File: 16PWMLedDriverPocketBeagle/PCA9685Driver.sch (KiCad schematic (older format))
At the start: 17 parts, among them P3 C A0 A1 A2 A3 A4 A5 A6 A7, P4 C B0 B1 B2 B3 B4 B5 B6 B7, U4 PCA9685, U5 TBD62X83A, U6 TBD62X83A

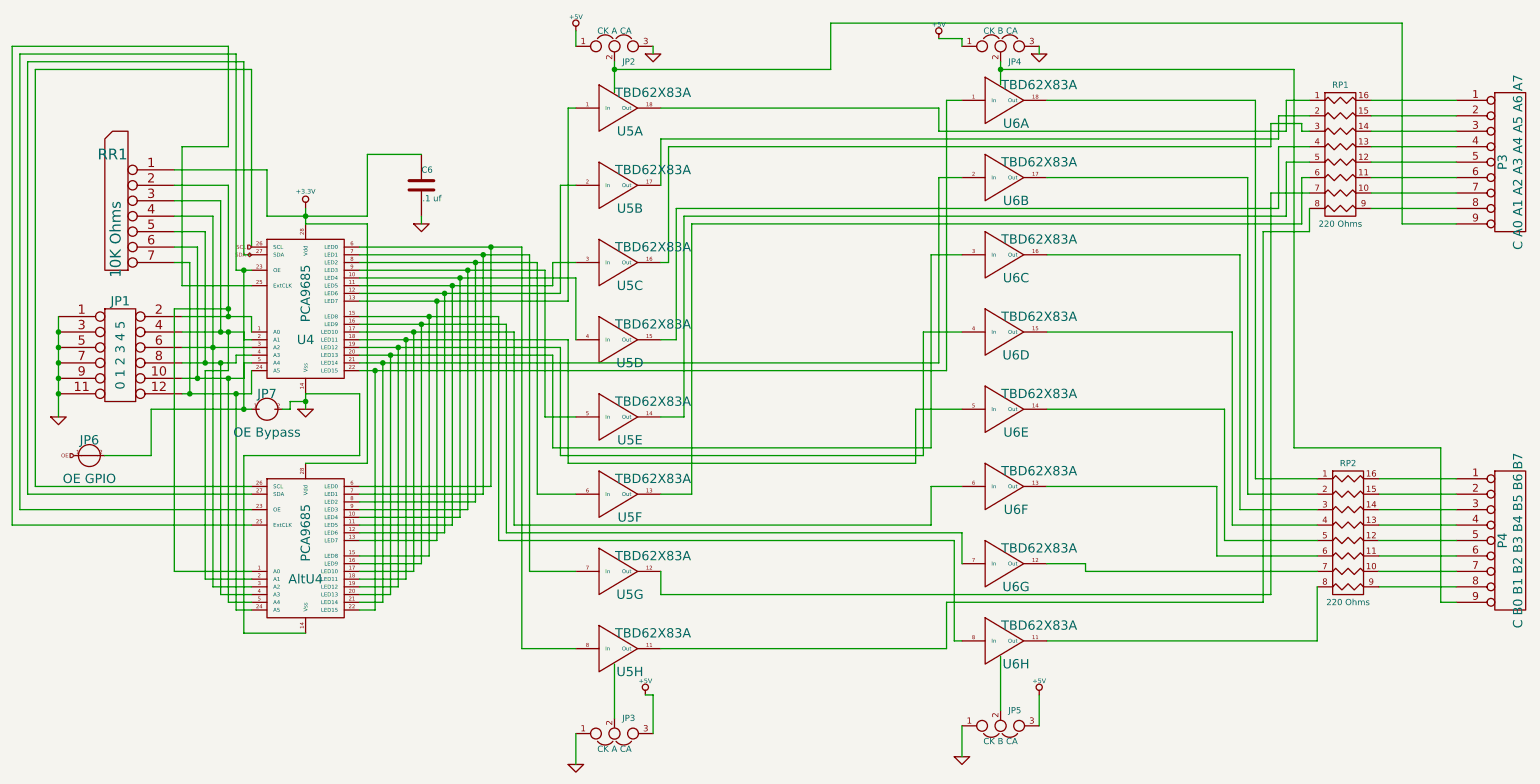
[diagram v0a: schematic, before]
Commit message: Convert the 16PWM Led Drivers to use 12V for the LEDs.
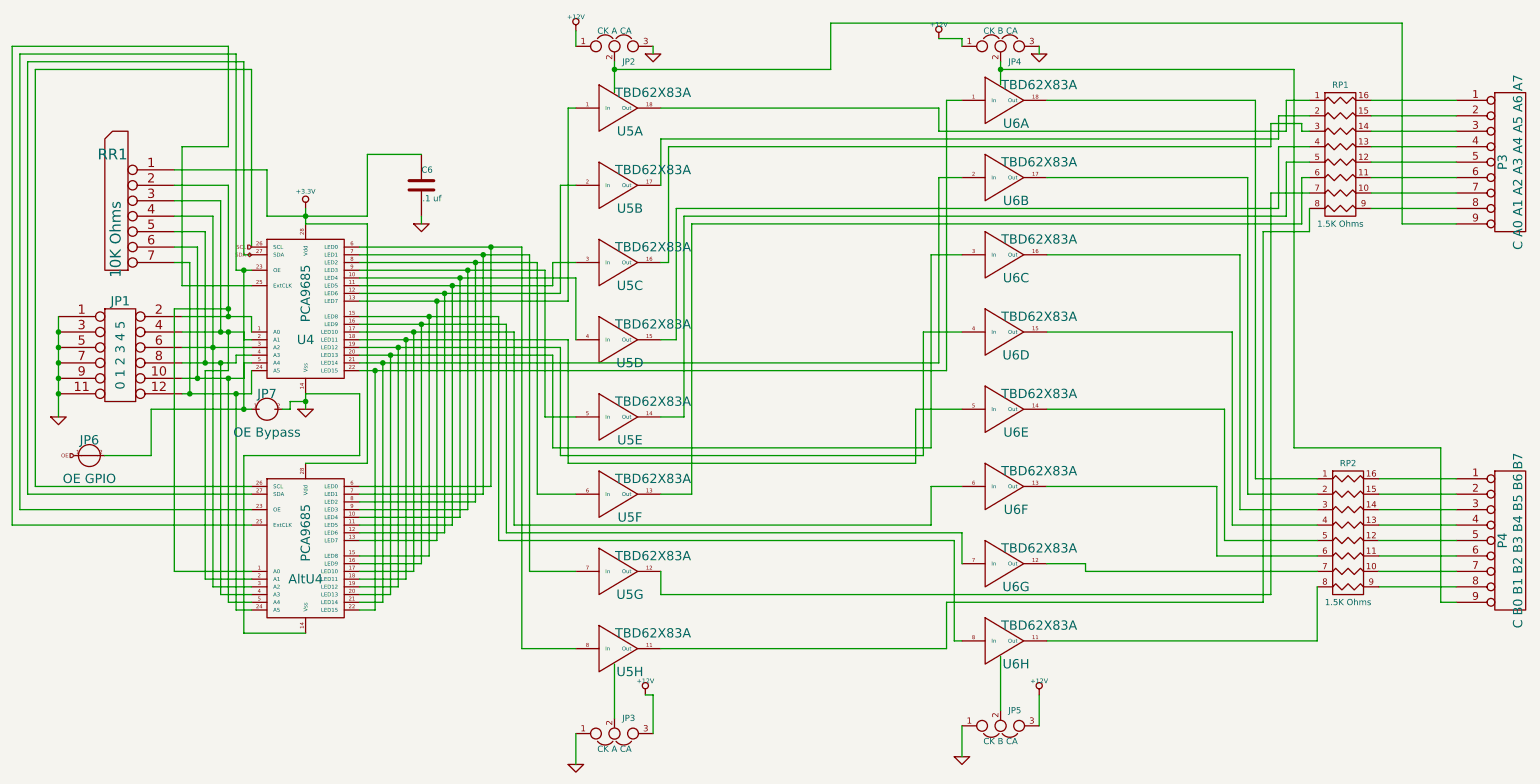
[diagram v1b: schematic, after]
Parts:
- RP1, RP2: value 220 Ohms -> 1.5K Ohms
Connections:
- net +5V renamed +12V
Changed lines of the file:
@@
 Sheet 3 3
 Title ""
-Date "11 mar 2019"
+Date "28 mar 2019"
 Rev ""
 Comp ""
@@
 OE
 $Comp
-L +3.3V #PWR015
+L +3.3V #PWR016
 U 1 1 5C840A94
 P 2800 1750
-F 0 "#PWR015" H 2800 1710 30  0001 C CNN
+F 0 "#PWR016" H 2800 1710 30  0001 C CNN
 F 1 "+3.3V" H 2800 1860 30  0000 C CNN
 F 2 "" H 2800 1750 60  0000 C CNN
@@
 $EndComp
 $Comp
-L GND #PWR016
+L GND #PWR017
 U 1 1 5C840AA3
 P 2800 3050
-F 0 "#PWR016" H 2800 3050 30  0001 C CNN
+F 0 "#PWR017" H 2800 3050 30  0001 C CNN
 F 1 "GND" H 2800 2980 30  0001 C CNN
 F 2 "" H 2800 3050 60  0000 C CNN
@@
 $EndComp
 $Comp
-L GND #PWR017
+L GND #PWR018
 U 1 1 5C840AF9
 P 3550 1850
-F 0 "#PWR017" H 3550 1850 30  0001 C CNN
+F 0 "#PWR018" H 3550 1850 30  0001 C CNN
 F 1 "GND" H 3550 1780 30  0001 C CNN
 F 2 "" H 3550 1850 60  0000 C CNN
@@
 P 9500 1400
 F 0 "RP1" H 9500 1850 40  0000 C CNN
-F 1 "220 Ohms" H 9500 950 40  0000 C CNN
+F 1 "1.5K Ohms" H 9500 950 40  0000 C CNN
 F 2 "~" H 9500 1400 60  0000 C CNN
 F 3 "~" H 9500 1400 60  0000 C CNN
@@
 P 9550 3850
 F 0 "RP2" H 9550 4300 40  0000 C CNN
-F 1 "220 Ohms" H 9550 3400 40  0000 C CNN
+F 1 "1.5K Ohms" H 9550 3400 40  0000 C CNN
 F 2 "~" H 9550 3850 60  0000 C CNN
 F 3 "~" H 9550 3850 60  0000 C CNN
@@
 $EndComp
 $Comp
-L +5V #PWR018
+L +12V #PWR019
 U 1 1 5C84283A
 P 4550 600
-F 0 "#PWR018" H 4550 690 20  0001 C CNN
-F 1 "+5V" H 4550 690 30  0000 C CNN
+F 0 "#PWR019" H 4550 690 20  0001 C CNN
+F 1 "+12V" H 4550 690 30  0000 C CNN
 F 2 "" H 4550 600 60  0000 C CNN
 F 3 "" H 4550 600 60  0000 C CNN
@@
 $EndComp
 $Comp
-L +5V #PWR019
+L +12V #PWR020
 U 1 1 5C842849
 P 6900 650
-F 0 "#PWR019" H 6900 740 20  0001 C CNN
-F 1 "+5V" H 6900 740 30  0000 C CNN
+F 0 "#PWR020" H 6900 740 20  0001 C CNN
+F 1 "+12V" H 6900 740 30  0000 C CNN
 F 2 "" H 6900 650 60  0000 C CNN
 F 3 "" H 6900 650 60  0000 C CNN
@@
 $EndComp
 $Comp
-L +5V #PWR020
+L +12V #PWR021
 U 1 1 5C842858
 P 7550 4900
-F 0 "#PWR020" H 7550 4990 20  0001 C CNN
-F 1 "+5V" H 7550 4990 30  0000 C CNN
+F 0 "#PWR021" H 7550 4990 20  0001 C CNN
+F 1 "+12V" H 7550 4990 30  0000 C CNN
 F 2 "" H 7550 4900 60  0000 C CNN
 F 3 "" H 7550 4900 60  0000 C CNN
@@
 $EndComp
 $Comp
-L +5V #PWR021
+L +12V #PWR022
 U 1 1 5C842867
 P 5000 4900
-F 0 "#PWR021" H 5000 4990 20  0001 C CNN
-F 1 "+5V" H 5000 4990 30  0000 C CNN
+F 0 "#PWR022" H 5000 4990 20  0001 C CNN
+F 1 "+12V" H 5000 4990 30  0000 C CNN
 F 2 "" H 5000 4900 60  0000 C CNN
 F 3 "" H 5000 4900 60  0000 C CNN
@@
 $EndComp
 $Comp
-L GND #PWR022
+L GND #PWR023
 U 1 1 5C842876
 P 4550 5350
-F 0 "#PWR022" H 4550 5350 30  0001 C CNN
+F 0 "#PWR023" H 4550 5350 30  0001 C CNN
 F 1 "GND" H 4550 5280 30  0001 C CNN
 F 2 "" H 4550 5350 60  0000 C CNN
@@
 $EndComp
 $Comp
-L GND #PWR023
+L GND #PWR024
 U 1 1 5C842885
 P 7050 5300
-F 0 "#PWR023" H 7050 5300 30  0001 C CNN
+F 0 "#PWR024" H 7050 5300 30  0001 C CNN
 F 1 "GND" H 7050 5230 30  0001 C CNN
 F 2 "" H 7050 5300 60  0000 C CNN
@@
 $EndComp
 $Comp
-L GND #PWR024
+L GND #PWR025
 U 1 1 5C842894
 P 7550 750
-F 0 "#PWR024" H 7550 750 30  0001 C CNN
+F 0 "#PWR025" H 7550 750 30  0001 C CNN
 F 1 "GND" H 7550 680 30  0001 C CNN
 F 2 "" H 7550 750 60  0000 C CNN
@@
 $EndComp
 $Comp
-L GND #PWR025
+L GND #PWR026
 U 1 1 5C8428A3
 P 5050 750
-F 0 "#PWR025" H 5050 750 30  0001 C CNN
+F 0 "#PWR026" H 5050 750 30  0001 C CNN
 F 1 "GND" H 5050 680 30  0001 C CNN
 F 2 "" H 5050 750 60  0000 C CNN
@@
 $EndComp
 $Comp
-L GND #PWR026
+L GND #PWR027
 U 1 1 5C84279D
 P 1200 3100
-F 0 "#PWR026" H 1200 3100 30  0001 C CNN
+F 0 "#PWR027" H 1200 3100 30  0001 C CNN
 F 1 "GND" H 1200 3030 30  0001 C CNN
 F 2 "" H 1200 3100 60  0000 C CNN

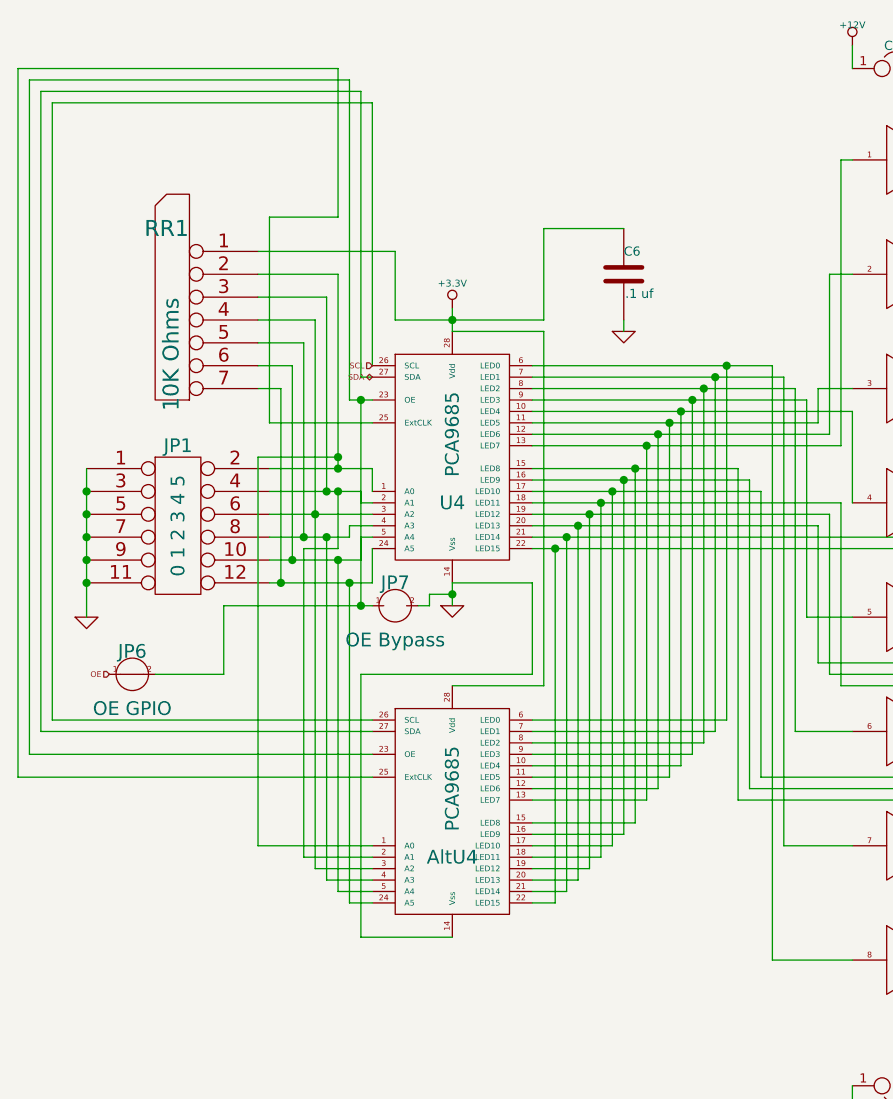
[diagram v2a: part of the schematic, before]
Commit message: Remove unused DIP and add LED power terminals.
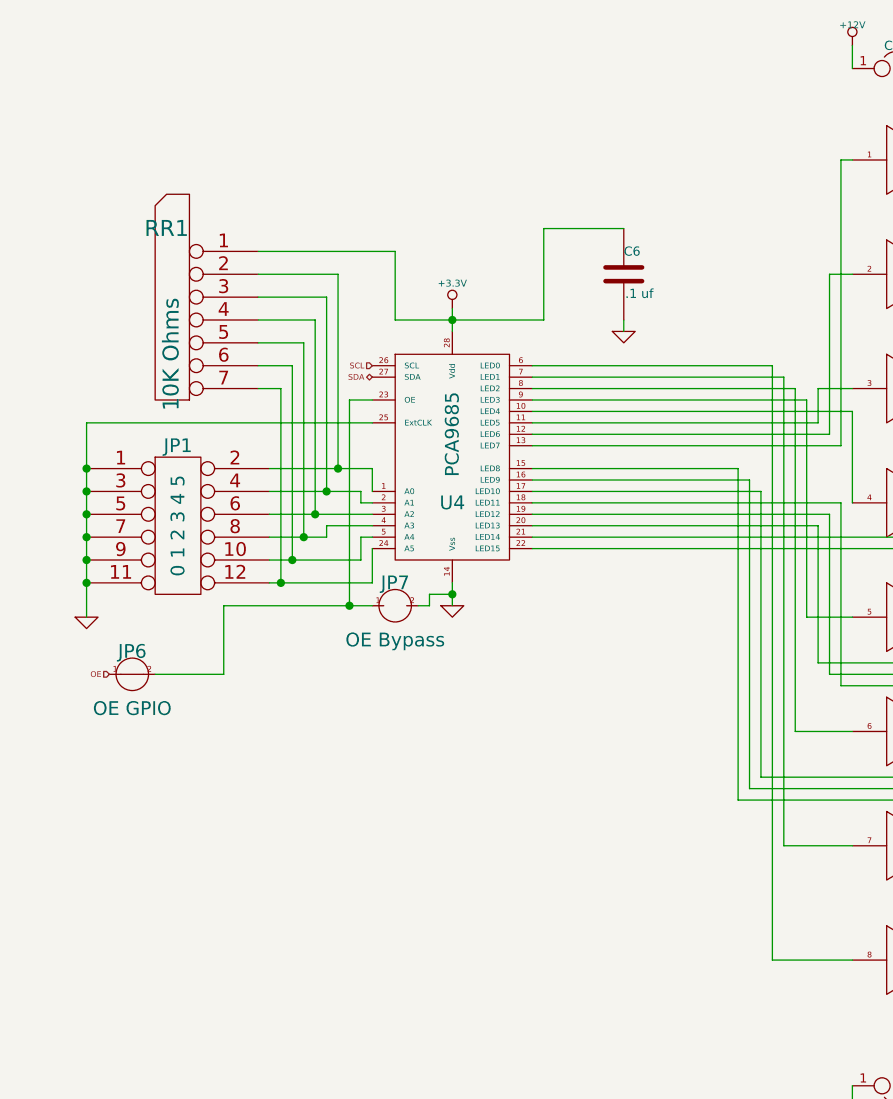
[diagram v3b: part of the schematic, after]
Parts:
- removed AltU4: PCA9685, ~, symbol PCA9685
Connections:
- net GND: now also U4.25 (ExtCLK)
- new net: JP1.4 (P4), RR1.3, U4.2 (A1)
- new net: JP6.2, JP7.1, U4.23 (OE)
- new net: JP1.10, RR1.6, U4.5 (A4)
